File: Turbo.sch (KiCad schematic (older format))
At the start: 24 parts, among them U12 74HCT27, U13 74HCT74, U14 74F86, U15 74F74, U16 74HCT04, U17 74HCT112, U18 74F157, U19 74F157

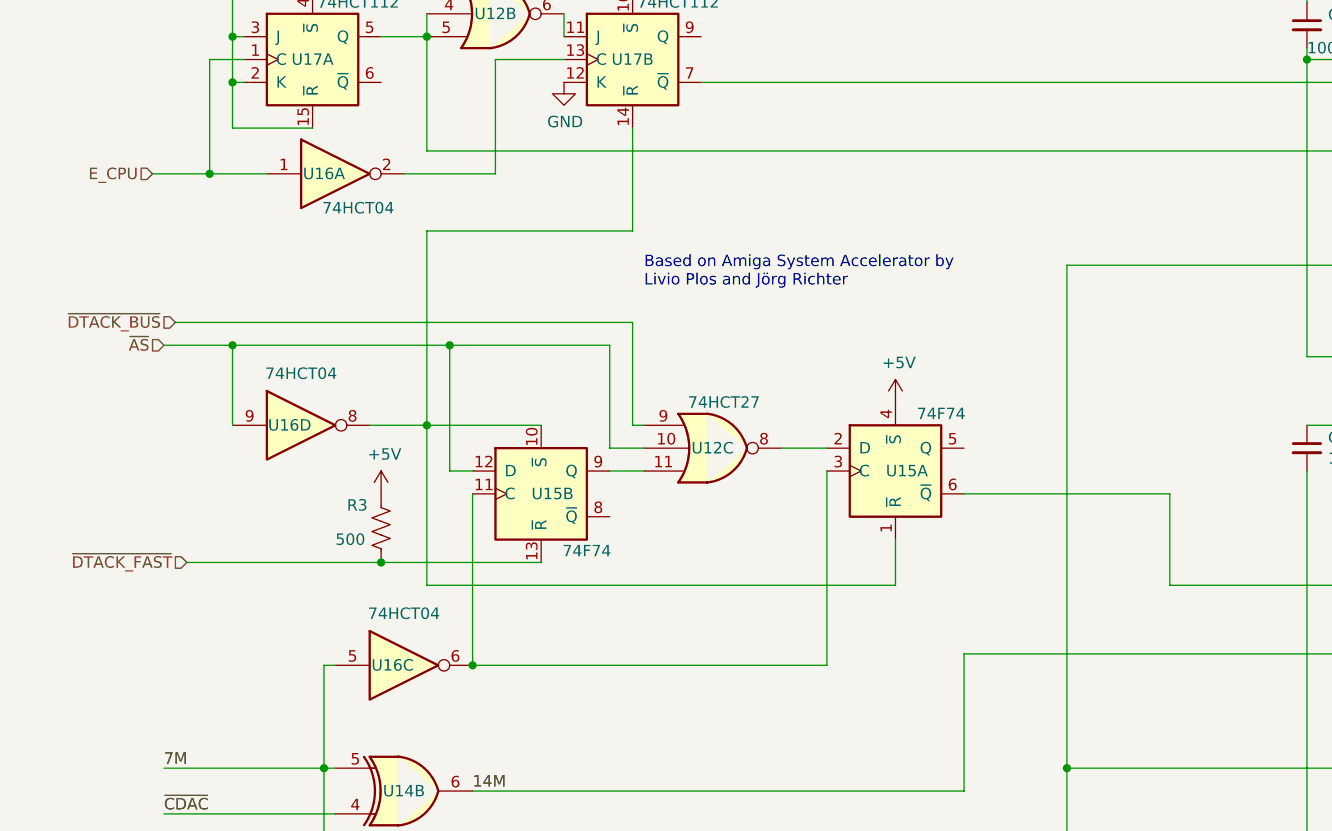
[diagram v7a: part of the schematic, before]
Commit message: new DTACK delay in schematics
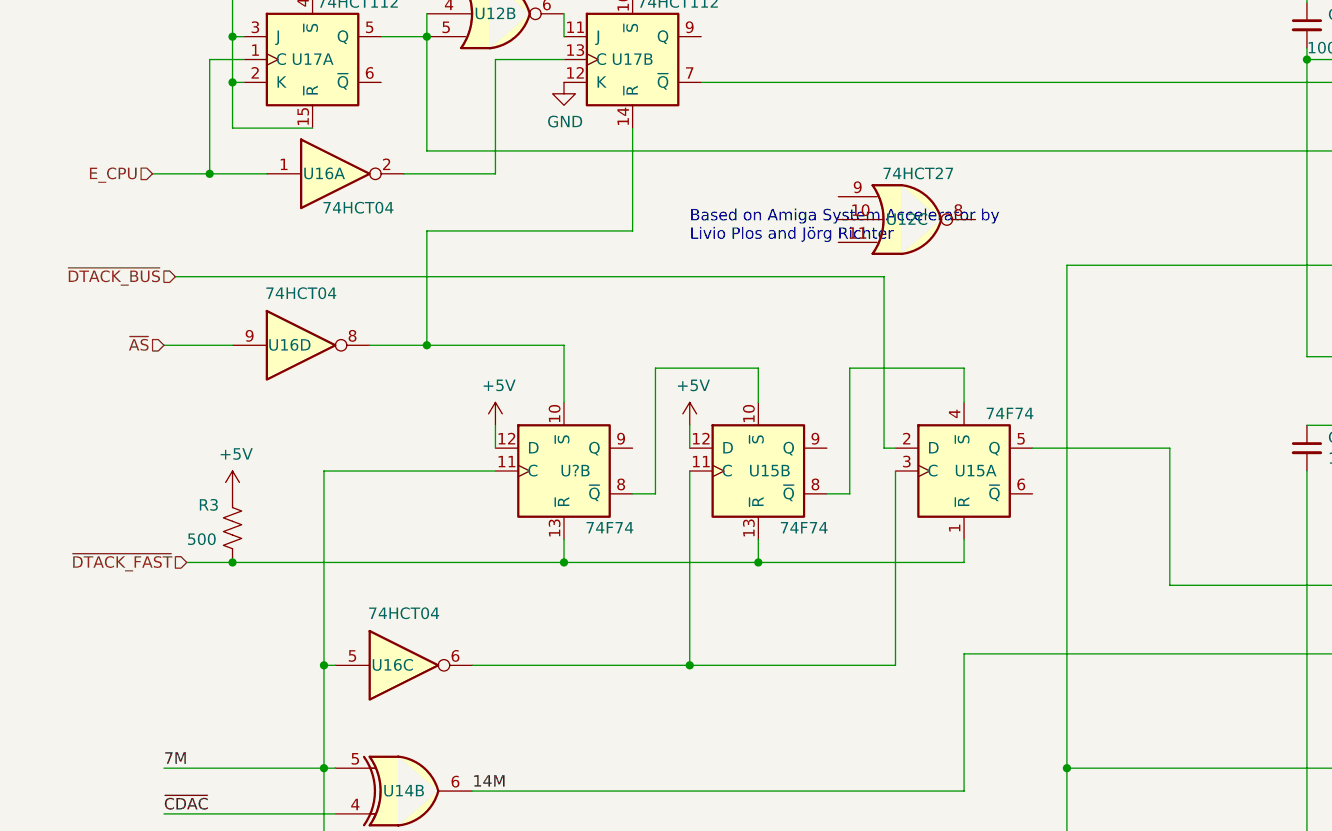
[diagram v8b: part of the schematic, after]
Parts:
- added U?: 74F74, Package_DIP:DIP-14_W7.62mm, symbol 74:74HC74
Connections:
- net +5V: now also U15.12 (D), U?.12 (D); no longer U15.4 (~S)
- net 7M: now also U?.11 (C)
- net ~AS: no longer U12.10, U15.12 (D)
- net ~DTACK_BUS: now also U15.2 (D); no longer U12.9
- net ~DTACK_FAST: now also U15.1 (~R), U?.13 (~R)
- net at U16.8, U17.14 (~R): now also U?.10 (~S); no longer U15.1 (~R), U15.10 (~S)
- net at U12.8: no longer U15.2 (D)
- net at U15.5 (Q): now also U19.6 (I1b)
- net at U15.6 (~Q): no longer U19.6 (I1b)
- net at U15.8 (~Q): now also U15.4 (~S)
- net at U15.9 (Q): no longer U12.11
- new net: U15.10 (~S), U?.8 (~Q)
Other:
- moved on the sheet: R3, U12C, U15A, U15B, U16D
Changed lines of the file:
@@
 Comment4 ""
 $EndDescr
-Text HLabel 1100 2650 0    50   Input ~ 0
+Text HLabel 1100 2450 0    50   Input ~ 0
 ~DTACK_BUS
 Text HLabel 1000 1000 0    50   Input ~ 0
@@
 L 74:74HC74 U15
 U 1 1 606CEE81
-P 4250 3300
-F 0 "U15" H 4300 3300 50  0000 C CNN
-F 1 "74F74" H 4450 3550 50  0000 C CNN
-F 2 "Package_DIP:DIP-14_W7.62mm" H 4250 3300 50  0001 C CNN
-F 3 "74xx/74hc_hct74.pdf" H 4250 3300 50  0001 C CNN
-	1    4250 3300
+P 4550 3300
+F 0 "U15" H 4600 3300 50  0000 C CNN
+F 1 "74F74" H 4750 3550 50  0000 C CNN
+F 2 "Package_DIP:DIP-14_W7.62mm" H 4550 3300 50  0001 C CNN
+F 3 "74xx/74hc_hct74.pdf" H 4550 3300 50  0001 C CNN
+	1    4550 3300
 	1    0    0    -1
 $EndComp
@@
 L 74:74HC74 U15
 U 2 1 606CFA45
-P 2700 3400
-F 0 "U15" H 2750 3400 50  0000 C CNN
-F 1 "74F74" H 2900 3150 50  0000 C CNN
-F 2 "Package_DIP:DIP-14_W7.62mm" H 2700 3400 50  0001 C CNN
-F 3 "74xx/74hc_hct74.pdf" H 2700 3400 50  0001 C CNN
-	2    2700 3400
+P 3650 3300
+F 0 "U15" H 3700 3300 50  0000 C CNN
+F 1 "74F74" H 3850 3050 50  0000 C CNN
+F 2 "Package_DIP:DIP-14_W7.62mm" H 3650 3300 50  0001 C CNN
+F 3 "74xx/74hc_hct74.pdf" H 3650 3300 50  0001 C CNN
+	2    3650 3300
 	1    0    0    -1
 $EndComp
@@
 L 74:74HCT04 U16
 U 4 1 606DE635
-P 1650 3100
-F 0 "U16" H 1600 3100 50  0000 C CNN
-F 1 "74HCT04" H 1650 3326 50  0000 C CNN
-F 2 "Package_DIP:DIP-14_W7.62mm" H 1650 3100 50  0001 C CNN
-F 3 "https://assets.nexperia.com/documents/data-sheet/74HC_HCT04.pdf" H 1650 3100 50  0001 C CNN
-	4    1650 3100
+P 1650 2750
+F 0 "U16" H 1600 2750 50  0000 C CNN
+F 1 "74HCT04" H 1650 2976 50  0000 C CNN
+F 2 "Package_DIP:DIP-14_W7.62mm" H 1650 2750 50  0001 C CNN
+F 3 "https://assets.nexperia.com/documents/data-sheet/74HC_HCT04.pdf" H 1650 2750 50  0001 C CNN
+	4    1650 2750
 	1    0    0    -1
 $EndComp
@@
 L 74:74LS27 U12
 U 3 1 606E87B7
-P 3450 3200
-F 0 "U12" H 3450 3200 50  0000 C CNN
-F 1 "74HCT27" H 3500 3400 50  0000 C CNN
-F 2 "Package_DIP:DIP-14_W7.62mm" H 3450 3200 50  0001 C CNN
-F 3 "http://www.ti.com/lit/gpn/sn74LS27" H 3450 3200 50  0001 C CNN
-	3    3450 3200
+P 4300 2200
+F 0 "U12" H 4300 2200 50  0000 C CNN
+F 1 "74HCT27" H 4350 2400 50  0000 C CNN
+F 2 "Package_DIP:DIP-14_W7.62mm" H 4300 2200 50  0001 C CNN
+F 3 "http://www.ti.com/lit/gpn/sn74LS27" H 4300 2200 50  0001 C CNN
+	3    4300 2200
 	1    0    0    -1
 $EndComp
@@
 $EndComp
 Wire Wire Line
-	3000 3300 3150 3300
-Wire Wire Line
-	3150 3200 3000 3200
-Wire Wire Line
-	3000 3200 3000 2750
-Wire Wire Line
-	3000 2750 2300 2750
-Wire Wire Line
-	3150 3100 3100 3100
-Wire Wire Line
-	3100 3100 3100 2650
-Wire Wire Line
-	1100 2650 3100 2650
-Wire Wire Line
-	2300 2750 2300 3300
-Wire Wire Line
-	2300 3300 2400 3300
-Connection ~ 2300 2750
-Wire Wire Line
-	2300 2750 1350 2750
-Wire Wire Line
-	1350 2750 1350 3100
-Connection ~ 1350 2750
+	1100 2450 4200 2450
 Wire Wire Line
 	1350 2750 1050 2750
 Wire Wire Line
-	1150 3700 2000 3700
-Wire Wire Line
-	1950 3100 2200 3100
-Wire Wire Line
-	2200 3100 2200 3800
-Wire Wire Line
-	2200 3800 4250 3800
-Connection ~ 2200 3100
-Wire Wire Line
-	2200 3100 2700 3100
-Wire Wire Line
-	4250 3800 4250 3600
-Wire Wire Line
-	3950 4150 3950 3300
-Wire Wire Line
-	2400 3400 2400 4150
-Connection ~ 2400 4150
-Wire Wire Line
-	2400 4150 3950 4150
+	1150 3700 1350 3700
+Wire Wire Line
+	1950 2750 2200 2750
+Wire Wire Line
+	4250 4150 4250 3300
+Wire Wire Line
+	2400 4150 3350 4150
 $Comp
 L OpenAmiga2000CoproAdapter-rescue:GND-power #PWR?
@@
 L device:R_US R?
 U 1 1 60718397
-P 2000 3550
+P 1350 3550
 AR Path="/6068F728/60718397" Ref="R?"  Part="1"
 AR Path="/606B7AE6/60718397" Ref="R3"  Part="1"
-F 0 "R3" H 1850 3650 50  0000 L CNN
-F 1 "500" H 1800 3500 50  0000 L CNN
-F 2 "Resistor_THT:R_Axial_DIN0411_L9.9mm_D3.6mm_P12.70mm_Horizontal" V 2040 3540 50  0001 C CNN
-F 3 "~" H 2000 3550 50  0001 C CNN
-	1    2000 3550
+F 0 "R3" H 1200 3650 50  0000 L CNN
+F 1 "500" H 1150 3500 50  0000 L CNN
+F 2 "Resistor_THT:R_Axial_DIN0411_L9.9mm_D3.6mm_P12.70mm_Horizontal" V 1390 3540 50  0001 C CNN
+F 3 "~" H 1350 3550 50  0001 C CNN
+	1    1350 3550
 	1    0    0    -1
 $EndComp
@@
 L OpenAmiga2000CoproAdapter-rescue:+5V-power #PWR?
 U 1 1 6071839D
-P 2000 3400
+P 1350 3400
 AR Path="/6071839D" Ref="#PWR?"  Part="1"
 AR Path="/6068F728/6071839D" Ref="#PWR?"  Part="1"
 AR Path="/606B7AE6/6071839D" Ref="#PWR0124"  Part="1"
-F 0 "#PWR0124" H 2000 3250 50  0001 C CNN
-F 1 "+5V" H 2015 3573 50  0000 C CNN
-F 2 "" H 2000 3400 50  0001 C CNN
-F 3 "" H 2000 3400 50  0001 C CNN
-	1    2000 3400
-	1    0    0    -1
-$EndComp
-$Comp
-L OpenAmiga2000CoproAdapter-rescue:+5V-power #PWR?
-U 1 1 60718B8E
-P 4250 3000
-AR Path="/60718B8E" Ref="#PWR?"  Part="1"
-AR Path="/6068F728/60718B8E" Ref="#PWR?"  Part="1"
-AR Path="/606B7AE6/60718B8E" Ref="#PWR0125"  Part="1"
-F 0 "#PWR0125" H 4250 2850 50  0001 C CNN
-F 1 "+5V" H 4265 3173 50  0000 C CNN
-F 2 "" H 4250 3000 50  0001 C CNN
-F 3 "" H 4250 3000 50  0001 C CNN
-	1    4250 3000
-	1    0    0    -1
-$EndComp
-Connection ~ 2000 3700
-Wire Wire Line
-	2000 3700 2700 3700
+F 0 "#PWR0124" H 1350 3250 50  0001 C CNN
+F 1 "+5V" H 1365 3573 50  0000 C CNN
+F 2 "" H 1350 3400 50  0001 C CNN
+F 3 "" H 1350 3400 50  0001 C CNN
+	1    1350 3400
+	1    0    0    -1
+$EndComp
 $Comp
 L 74:74LS112 U17
@@
 $EndComp
 Wire Wire Line
-	2200 3100 2200 2250
+	2200 2750 2200 2250
 Wire Wire Line
 	2200 2250 3100 2250
@@
 Wire Wire Line
 	2200 1400 2200 1900
-Text Notes 3150 2500 0    50   ~ 0
+Text Notes 3350 2300 0    50   ~ 0
 Based on Amiga System Accelerator by\nLivio Plos and Jörg Richter
-Wire Wire Line
-	1800 4150 1750 4150
 Connection ~ 1750 4600
 Wire Wire Line
@@
 	2200 1900 6800 1900
 Wire Wire Line
-	4550 3400 5450 3400
-Wire Wire Line
 	6800 2100 6800 2200
 Connection ~ 6800 2500
@@
 Text HLabel 6800 1800 0    50   Input ~ 0
 E_CPU
-Wire Wire Line
-	1750 4150 1750 4600
 Text HLabel 6800 3700 0    50   Input ~ 0
 ~DTACK_BUS
@@
 	4550 4100 4550 4700
 Wire Wire Line
-	5450 3800 5450 3400
-Wire Wire Line
 	5450 3800 6800 3800
 Text HLabel 6800 4300 0    50   Input ~ 0
@@
 Wire Wire Line
 	5000 4600 5000 5600
-Wire Wire Line
-	3750 3200 3950 3200
 Wire Wire Line
 	2500 1500 2500 2000
@@
 Text Label 1050 4800 0    50   ~ 0
 ~CDAC
+Connection ~ 1350 3700
+Connection ~ 1750 4150
+Wire Wire Line
+	1750 4150 1750 4600
+Wire Wire Line
+	1800 4150 1750 4150
+Wire Wire Line
+	4850 3200 5450 3200
+Wire Wire Line
+	5450 3200 5450 3800
+Wire Wire Line
+	4250 3200 4200 3200
+Wire Wire Line
+	4200 2450 4200 3200
+Wire Wire Line
+	3950 3400 4050 3400
+Wire Wire Line
+	4050 3400 4050 2850
+Wire Wire Line
+	4050 2850 4550 2850
+Wire Wire Line
+	4550 2850 4550 3000
+$Comp
+L 74:74HC74 U?
+U 2 1 6107A182
+P 2800 3300
+F 0 "U?" H 2850 3300 50  0000 C CNN
+F 1 "74F74" H 3000 3050 50  0000 C CNN
+F 2 "Package_DIP:DIP-14_W7.62mm" H 2800 3300 50  0001 C CNN
+F 3 "74xx/74hc_hct74.pdf" H 2800 3300 50  0001 C CNN
+	2    2800 3300
+	1    0    0    -1
+$EndComp
+Wire Wire Line
+	3650 3700 3650 3600
+Wire Wire Line
+	1350 3700 2800 3700
+Wire Wire Line
+	3350 3300 3350 4150
+Connection ~ 3350 4150
+Wire Wire Line
+	3350 4150 4250 4150
+Wire Wire Line
+	2800 2750 2800 3000
+Wire Wire Line
+	3100 3400 3200 3400
+Wire Wire Line
+	3200 3400 3200 2850
+Wire Wire Line
+	3200 2850 3650 2850
+Wire Wire Line
+	3650 2850 3650 3000
+Wire Wire Line
+	2800 3600 2800 3700
+Connection ~ 2800 3700
+Wire Wire Line
+	2800 3700 3650 3700
+$Comp
+L OpenAmiga2000CoproAdapter-rescue:+5V-power #PWR?
+U 1 1 610996B9
+P 3350 3100
+AR Path="/610996B9" Ref="#PWR?"  Part="1"
+AR Path="/6068F728/610996B9" Ref="#PWR?"  Part="1"
+AR Path="/606B7AE6/610996B9" Ref="#PWR?"  Part="1"
+F 0 "#PWR?" H 3350 2950 50  0001 C CNN
+F 1 "+5V" H 3365 3273 50  0000 C CNN
+F 2 "" H 3350 3100 50  0001 C CNN
+F 3 "" H 3350 3100 50  0001 C CNN
+	1    3350 3100
+	1    0    0    -1
+$EndComp
+$Comp
+L OpenAmiga2000CoproAdapter-rescue:+5V-power #PWR?
+U 1 1 6109A70F
+P 2500 3100
+AR Path="/6109A70F" Ref="#PWR?"  Part="1"
+AR Path="/6068F728/6109A70F" Ref="#PWR?"  Part="1"
+AR Path="/606B7AE6/6109A70F" Ref="#PWR?"  Part="1"
+F 0 "#PWR?" H 2500 2950 50  0001 C CNN
+F 1 "+5V" H 2515 3273 50  0000 C CNN
+F 2 "" H 2500 3100 50  0001 C CNN
+F 3 "" H 2500 3100 50  0001 C CNN
+	1    2500 3100
+	1    0    0    -1
+$EndComp
+Wire Wire Line
+	3350 3100 3350 3200
+Wire Wire Line
+	2500 3100 2500 3200
+Wire Wire Line
+	2500 3300 1750 3300
+Wire Wire Line
+	1750 3300 1750 4150
+Wire Wire Line
+	4550 3700 3650 3700
+Wire Wire Line
+	4550 3700 4550 3600
+Connection ~ 3650 3700
+Wire Wire Line
+	2200 2750 2800 2750
+Connection ~ 2200 2750
 $EndSCHEMATC
